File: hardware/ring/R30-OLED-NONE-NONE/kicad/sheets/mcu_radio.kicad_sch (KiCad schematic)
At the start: 4 parts, among them U1 ESP32-C3-MINI-1-N4

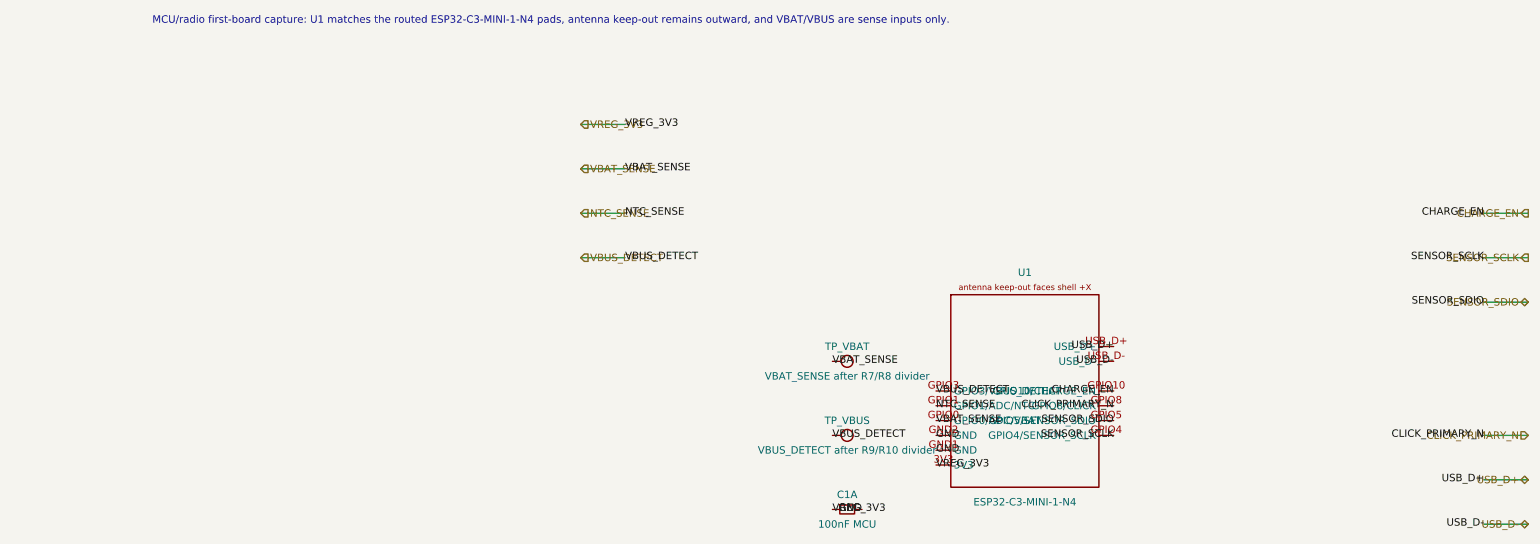
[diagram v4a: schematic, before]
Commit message: fix(r30): reconcile schematic net parity
Sensing mechanism: PAW3204 optical surface tracking.

Form factor and angle: R30 30-degree ring, OLED/NONE/NONE active lane.

Intended use: accessibility-first BLE HID pointing first-board validation.

BOM estimate: active R30 prototype remains about .30-.45, target about .
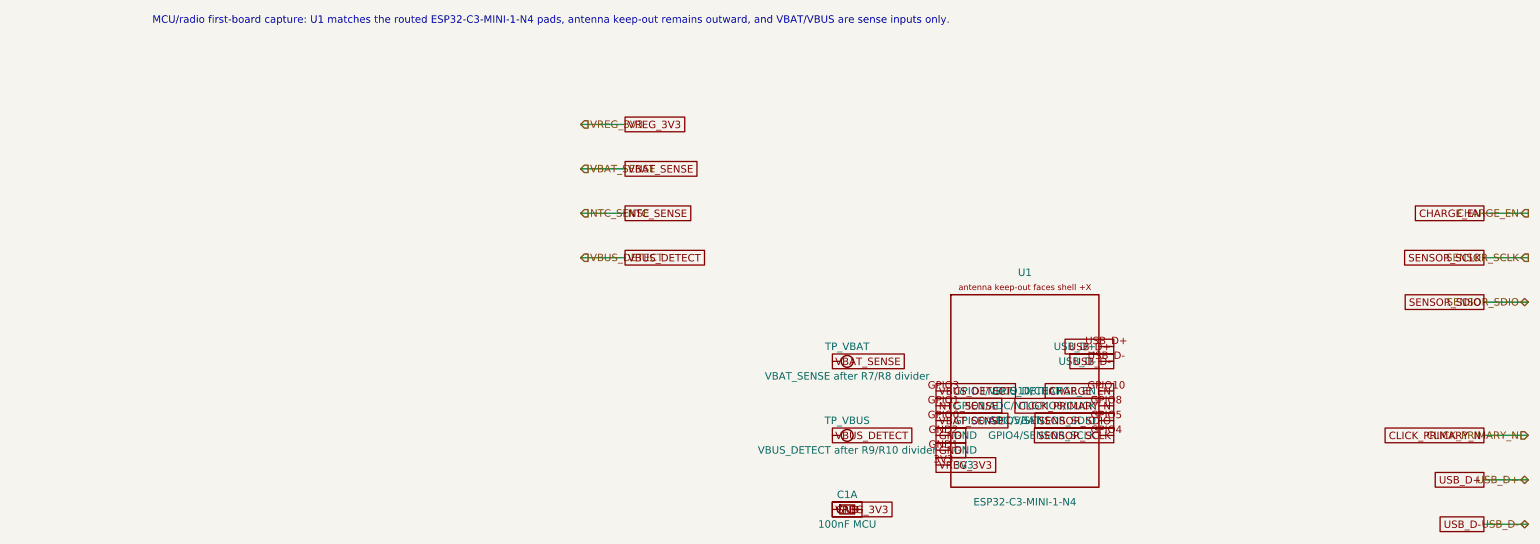
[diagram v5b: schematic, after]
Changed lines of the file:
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@@
   (wire (pts (xy 180.34 99.06) (xy 187.96 99.06)) (stroke (width 0) (type default) (color 0 0 0 0)))
   (wire (pts (xy 180.34 106.68) (xy 187.96 106.68)) (stroke (width 0) (type default) (color 0 0 0 0)))
-  (label "VREG_3V3" (at 33.02 38.1 0) (effects (font (size 1.27 1.27))))
-  (label "VBAT_SENSE" (at 33.02 45.72 0) (effects (font (size 1.27 1.27))))
-  (label "NTC_SENSE" (at 33.02 53.34 0) (effects (font (size 1.27 1.27))))
-  (label "VBUS_DETECT" (at 33.02 60.96 0) (effects (font (size 1.27 1.27))))
-  (label "CHARGE_EN" (at 180.34 53.34 180) (effects (font (size 1.27 1.27))))
-  (label "SENSOR_SCLK" (at 180.34 60.96 180) (effects (font (size 1.27 1.27))))
-  (label "SENSOR_SDIO" (at 180.34 68.58 180) (effects (font (size 1.27 1.27))))
-      (label "CLICK_PRIMARY_N" (at 180.34 91.44 180) (effects (font (size 1.27 1.27))))
-  (label "USB_D+" (at 180.34 99.06 180) (effects (font (size 1.27 1.27))))
-  (label "USB_D-" (at 180.34 106.68 180) (effects (font (size 1.27 1.27))))
+  (global_label "VREG_3V3" (shape passive) (at 33.02 38.1 0) (effects (font (size 1.27 1.27))))
+  (global_label "VBAT_SENSE" (shape passive) (at 33.02 45.72 0) (effects (font (size 1.27 1.27))))
+  (global_label "NTC_SENSE" (shape passive) (at 33.02 53.34 0) (effects (font (size 1.27 1.27))))
+  (global_label "VBUS_DETECT" (shape passive) (at 33.02 60.96 0) (effects (font (size 1.27 1.27))))
+  (global_label "CHARGE_EN" (shape passive) (at 180.34 53.34 180) (effects (font (size 1.27 1.27))))
+  (global_label "SENSOR_SCLK" (shape passive) (at 180.34 60.96 180) (effects (font (size 1.27 1.27))))
+  (global_label "SENSOR_SDIO" (shape passive) (at 180.34 68.58 180) (effects (font (size 1.27 1.27))))
+      (global_label "CLICK_PRIMARY_N" (shape passive) (at 180.34 91.44 180) (effects (font (size 1.27 1.27))))
+  (global_label "USB_D+" (shape passive) (at 180.34 99.06 180) (effects (font (size 1.27 1.27))))
+  (global_label "USB_D-" (shape passive) (at 180.34 106.68 180) (effects (font (size 1.27 1.27))))
   (symbol (lib_id "PowerFinger:ESP32-C3-MINI-1-N4_FirstBoard") (at 101.6 83.82 0) (unit 1)
     (in_bom yes) (on_board yes) (dnp no)
@@
     )
   )
-  (label "VREG_3V3" (at 86.36 96.52 0) (effects (font (size 1.27 1.27))))
-  (label "GND" (at 86.36 93.98 0) (effects (font (size 1.27 1.27))))
-  (label "GND" (at 86.36 91.44 0) (effects (font (size 1.27 1.27))))
-  (label "VBAT_SENSE" (at 86.36 88.9 0) (effects (font (size 1.27 1.27))))
-  (label "NTC_SENSE" (at 86.36 86.36 0) (effects (font (size 1.27 1.27))))
-  (label "VBUS_DETECT" (at 86.36 83.82 0) (effects (font (size 1.27 1.27))))
-  (label "SENSOR_SCLK" (at 116.84 91.44 180) (effects (font (size 1.27 1.27))))
-  (label "SENSOR_SDIO" (at 116.84 88.9 180) (effects (font (size 1.27 1.27))))
-  (label "CLICK_PRIMARY_N" (at 116.84 86.36 180) (effects (font (size 1.27 1.27))))
-  (label "CHARGE_EN" (at 116.84 83.82 180) (effects (font (size 1.27 1.27))))
-  (label "USB_D-" (at 116.84 78.74 180) (effects (font (size 1.27 1.27))))
-  (label "USB_D+" (at 116.84 76.2 180) (effects (font (size 1.27 1.27))))
-  (label "VREG_3V3" (at 68.58 104.14 0) (effects (font (size 1.27 1.27))))
-  (label "GND" (at 73.66 104.14 180) (effects (font (size 1.27 1.27))))
-  (label "VBAT_SENSE" (at 68.58 78.74 0) (effects (font (size 1.27 1.27))))
-  (label "VBUS_DETECT" (at 68.58 91.44 0) (effects (font (size 1.27 1.27))))
+  (global_label "VREG_3V3" (shape passive) (at 86.36 96.52 0) (effects (font (size 1.27 1.27))))
+  (global_label "GND" (shape passive) (at 86.36 93.98 0) (effects (font (size 1.27 1.27))))
+  (global_label "GND" (shape passive) (at 86.36 91.44 0) (effects (font (size 1.27 1.27))))
+  (global_label "VBAT_SENSE" (shape passive) (at 86.36 88.9 0) (effects (font (size 1.27 1.27))))
+  (global_label "NTC_SENSE" (shape passive) (at 86.36 86.36 0) (effects (font (size 1.27 1.27))))
+  (global_label "VBUS_DETECT" (shape passive) (at 86.36 83.82 0) (effects (font (size 1.27 1.27))))
+  (global_label "SENSOR_SCLK" (shape passive) (at 116.84 91.44 180) (effects (font (size 1.27 1.27))))
+  (global_label "SENSOR_SDIO" (shape passive) (at 116.84 88.9 180) (effects (font (size 1.27 1.27))))
+  (global_label "CLICK_PRIMARY_N" (shape passive) (at 116.84 86.36 180) (effects (font (size 1.27 1.27))))
+  (global_label "CHARGE_EN" (shape passive) (at 116.84 83.82 180) (effects (font (size 1.27 1.27))))
+  (global_label "USB_D-" (shape passive) (at 116.84 78.74 180) (effects (font (size 1.27 1.27))))
+  (global_label "USB_D+" (shape passive) (at 116.84 76.2 180) (effects (font (size 1.27 1.27))))
+  (global_label "VREG_3V3" (shape passive) (at 68.58 104.14 0) (effects (font (size 1.27 1.27))))
+  (global_label "GND" (shape passive) (at 73.66 104.14 180) (effects (font (size 1.27 1.27))))
+  (global_label "VBAT_SENSE" (shape passive) (at 68.58 78.74 0) (effects (font (size 1.27 1.27))))
+  (global_label "VBUS_DETECT" (shape passive) (at 68.58 91.44 0) (effects (font (size 1.27 1.27))))
   (sheet_instances
     (path "/" (page "1"))

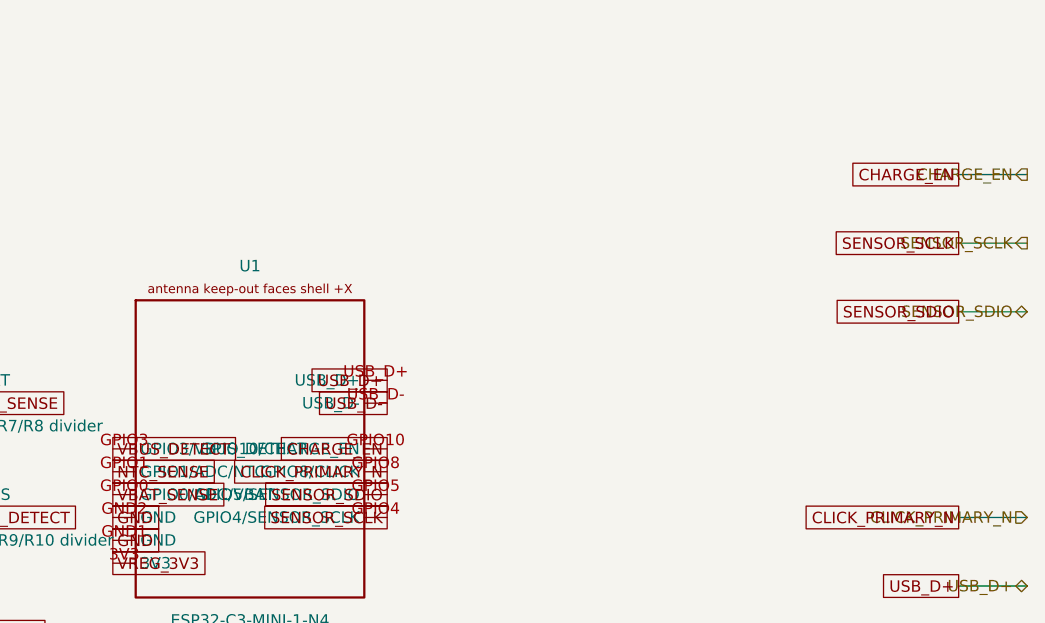
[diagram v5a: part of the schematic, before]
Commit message: feat(r30): cut service hardware blockers
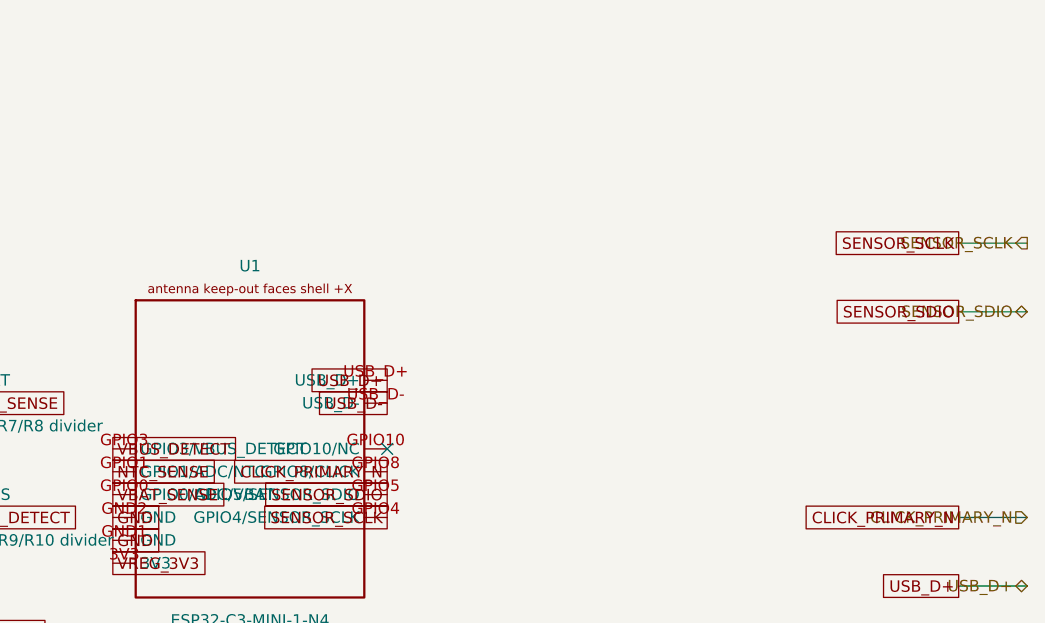
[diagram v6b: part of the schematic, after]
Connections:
- net CHARGE_EN: no longer names the net of U1.GPIO10 (GPIO10/NC)
- no-connect marks 0 -> 1
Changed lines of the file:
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@@
-    (effects (font (size 1.27 1.27)))
-  )
-  (hierarchical_label "CHARGE_EN" (shape output) (at 187.96 53.34 180)
     (effects (font (size 1.27 1.27)))
   )
@@
   (wire (pts (xy 25.4 53.34) (xy 33.02 53.34)) (stroke (width 0) (type default) (color 0 0 0 0)))
   (wire (pts (xy 25.4 60.96) (xy 33.02 60.96)) (stroke (width 0) (type default) (color 0 0 0 0)))
-  (wire (pts (xy 180.34 53.34) (xy 187.96 53.34)) (stroke (width 0) (type default) (color 0 0 0 0)))
   (wire (pts (xy 180.34 60.96) (xy 187.96 60.96)) (stroke (width 0) (type default) (color 0 0 0 0)))
   (wire (pts (xy 180.34 68.58) (xy 187.96 68.58)) (stroke (width 0) (type default) (color 0 0 0 0)))
@@
   (global_label "NTC_SENSE" (shape passive) (at 33.02 53.34 0) (effects (font (size 1.27 1.27))))
   (global_label "VBUS_DETECT" (shape passive) (at 33.02 60.96 0) (effects (font (size 1.27 1.27))))
-  (global_label "CHARGE_EN" (shape passive) (at 180.34 53.34 180) (effects (font (size 1.27 1.27))))
   (global_label "SENSOR_SCLK" (shape passive) (at 180.34 60.96 180) (effects (font (size 1.27 1.27))))
   (global_label "SENSOR_SDIO" (shape passive) (at 180.34 68.58 180) (effects (font (size 1.27 1.27))))
@@
   (global_label "SENSOR_SDIO" (shape passive) (at 116.84 88.9 180) (effects (font (size 1.27 1.27))))
   (global_label "CLICK_PRIMARY_N" (shape passive) (at 116.84 86.36 180) (effects (font (size 1.27 1.27))))
-  (global_label "CHARGE_EN" (shape passive) (at 116.84 83.82 180) (effects (font (size 1.27 1.27))))
+  (no_connect (at 116.84 83.82))
   (global_label "USB_D-" (shape passive) (at 116.84 78.74 180) (effects (font (size 1.27 1.27))))
   (global_label "USB_D+" (shape passive) (at 116.84 76.2 180) (effects (font (size 1.27 1.27))))
